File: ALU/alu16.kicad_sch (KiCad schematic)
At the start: 18 parts, among them U4 74LS181, U5 74LS181, U8 74LS181, U9 74LS181

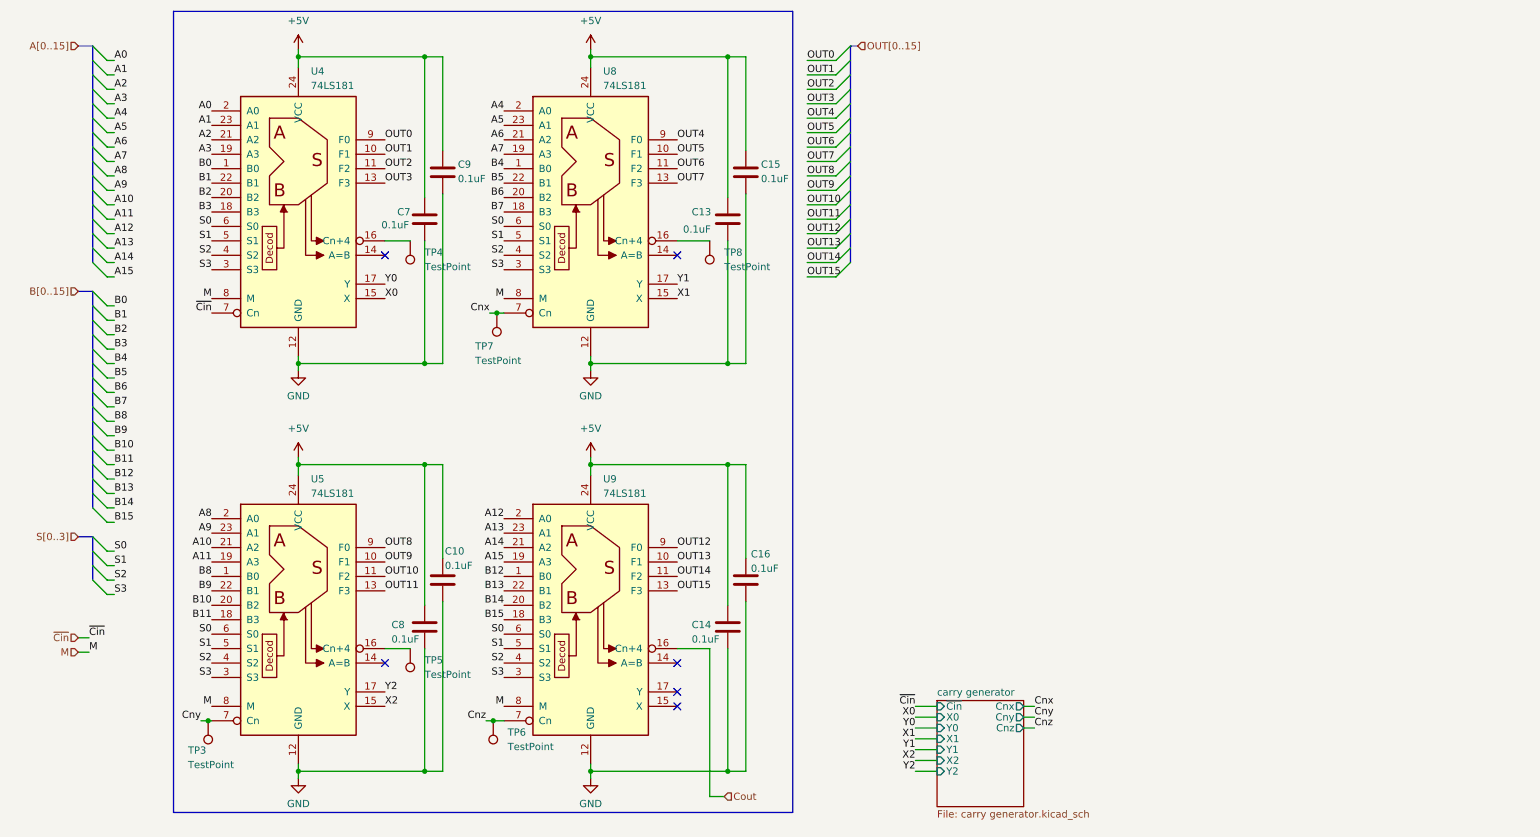
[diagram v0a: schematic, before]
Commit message: Updated ALU and moved common schematics to common/ for enhanced reusability
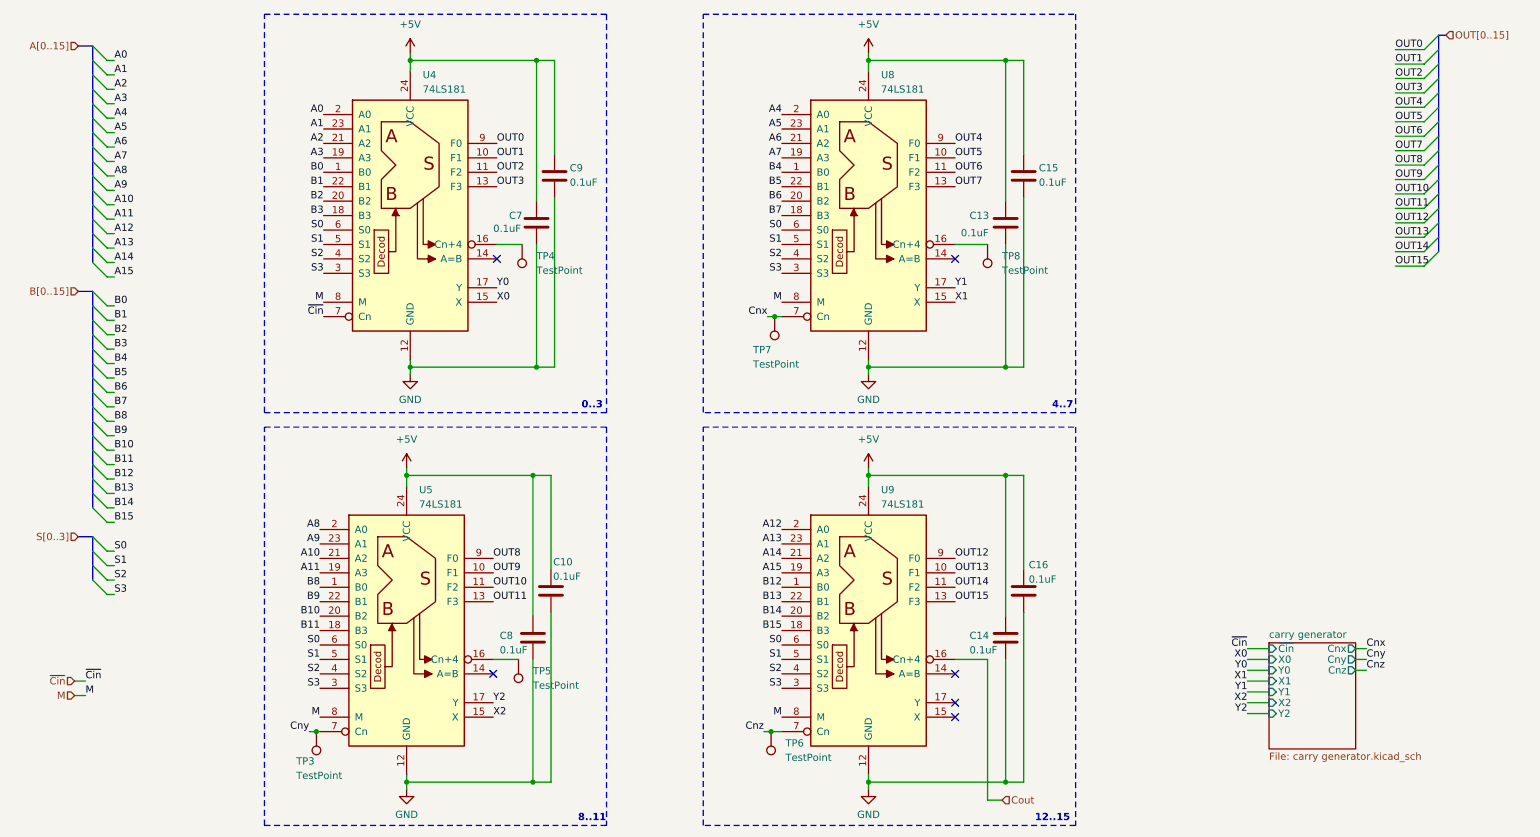
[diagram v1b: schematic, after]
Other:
- note added: "0..3"
- note added: "12..15"
- note added: "4..7"
- note added: "8..11"
- moved on the sheet: C10, C13, C14, C15, C16, C7, C8, C9, TP3, TP4, TP5, TP6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
